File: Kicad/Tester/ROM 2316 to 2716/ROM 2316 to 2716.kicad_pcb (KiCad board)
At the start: 2 copper layers, 19.8 x 30.5 mm, 6 parts, among them IC1 74LVC1G04GV,125, J1 2316 Right, J2 2316 Left, J3 2716 Left, J4 2716 Right

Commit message: Renamed HCP65 Power to W65C816 Power.
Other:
- board text added: "2316 to 2716 ROM Adapter"
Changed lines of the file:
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@@
 			(outputformat 1)
 			(mirror no)
-			(drillshape 1)
+			(drillshape 0)
 			(scaleselection 1)
-			(outputdirectory "")
+			(outputdirectory "ROM 2316 to 2716/")
 		)
 	)
@@
 		(layer "Edge.Cuts")
 	)
+	(gr_text "2316 to 2716\nROM Adapter"
+		(at 90.043 73.279 90)
+		(layer "F.SilkS")
+		(effects
+			(font
+				(size 1 1)
+				(thickness 0.2)
+				(bold yes)
+			)
+		)
+	)
 	(segment
 		(start 90.17 84.328)
@@
 	)
 	(segment
-		(start 97.9243 63.5)
-		(end 98.552 63.5)
-		(width 0.35)
-		(layer "F.Cu")
-		(net 1)
-	)
-	(segment
-		(start 96.52 63.5)
-		(end 97.883 63.5)
-		(width 0.35)
-		(layer "F.Cu")
-		(net 1)
-	)
-	(segment
 		(start 95.504 69.85)
 		(end 97.282 69.85)
@@
 	)
 	(segment
+		(start 96.52 63.5)
+		(end 98.552 63.5)
+		(width 1.1)
+		(layer "F.Cu")
+		(net 1)
+	)
+	(segment
 		(start 90.17 83.643)
 		(end 91.009 82.804)
@@
 	)
 	(segment
-		(start 97.883 63.5)
-		(end 97.9243 63.5)
-		(width 0.35)
-		(layer "F.Cu")
-		(net 1)
-	)
-	(segment
 		(start 94.996 65.024)
 		(end 94.996 69.342)
@@
 		(start 83.312 91.44)
 		(end 81.28 91.44)
-		(width 0.35)
+		(width 1.1)
 		(layer "F.Cu")
 		(net 2)
@@
 		(start 98.552 68.58)
 		(end 96.52 68.58)
-		(width 0.2)
+		(width 1.1)
 		(layer "F.Cu")
 		(net 6)
@@
 		(start 83.312 78.74)
 		(end 81.28 78.74)
-		(width 0.2)
+		(width 1.1)
 		(layer "F.Cu")
 		(net 7)
@@
 		(start 83.312 68.58)
 		(end 81.28 68.58)
-		(width 0.2)
+		(width 1.1)
 		(layer "F.Cu")
 		(net 8)
@@
 		(start 83.312 73.66)
 		(end 81.28 73.66)
-		(width 0.2)
+		(width 1.1)
 		(layer "F.Cu")
 		(net 9)
@@
 		(start 83.312 71.12)
 		(end 81.28 71.12)
-		(width 0.2)
+		(width 1.1)
 		(layer "F.Cu")
 		(net 10)
@@
 		(start 81.28 83.82)
 		(end 83.312 83.82)
-		(width 0.2)
+		(width 1.1)
 		(layer "F.Cu")
 		(net 11)
@@
 		(start 96.52 73.66)
 		(end 98.552 73.66)
-		(width 0.2)
+		(width 1.1)
 		(layer "F.Cu")
 		(net 12)
@@
 		(start 96.520001 88.9)
 		(end 98.552001 88.9)
-		(width 0.2)
+		(width 1.1)
 		(layer "F.Cu")
 		(net 13)
@@
 		(start 96.52 91.44)
 		(end 98.552 91.44)
-		(width 0.2)
+		(width 1.1)
 		(layer "F.Cu")
 		(net 14)
@@
 		(start 83.312 76.2)
 		(end 81.28 76.2)
-		(width 0.2)
+		(width 1.1)
 		(layer "F.Cu")
 		(net 15)
@@
 		(start 81.28 63.5)
 		(end 83.312 63.5)
-		(width 0.2)
+		(width 1.1)
 		(layer "F.Cu")
 		(net 16)
@@
 		(start 83.312 86.36)
 		(end 81.28 86.36)
-		(width 0.2)
+		(width 1.1)
 		(layer "F.Cu")
 		(net 17)
@@
 		(start 98.552 83.82)
 		(end 96.52 83.82)
-		(width 0.2)
+		(width 1.1)
 		(layer "F.Cu")
 		(net 18)
@@
 		(start 96.520001 66.04)
 		(end 98.552001 66.04)
-		(width 0.2)
+		(width 1.1)
 		(layer "F.Cu")
 		(net 19)
@@
 		(start 98.552 76.199999)
 		(end 96.52 76.199999)
-		(width 0.2)
+		(width 1.1)
 		(layer "F.Cu")
 		(net 20)
@@
 		(start 81.28 81.28)
 		(end 83.312 81.28)
-		(width 0.2)
+		(width 1.1)
 		(layer "F.Cu")
 		(net 21)
@@
 		(start 83.312 88.9)
 		(end 81.28 88.9)
-		(width 0.2)
+		(width 1.1)
 		(layer "F.Cu")
 		(net 22)
@@
 		(start 98.552 81.28)
 		(end 96.52 81.28)
-		(width 0.2)
+		(width 1.1)
 		(layer "F.Cu")
 		(net 23)
@@
 		(start 98.552 86.36)
 		(end 96.52 86.36)
-		(width 0.2)
+		(width 1.1)
 		(layer "F.Cu")
 		(net 24)
@@
 		(start 81.28 66.04)
 		(end 83.312 66.04)
-		(width 0.2)
+		(width 1.1)
 		(layer "F.Cu")
 		(net 25)

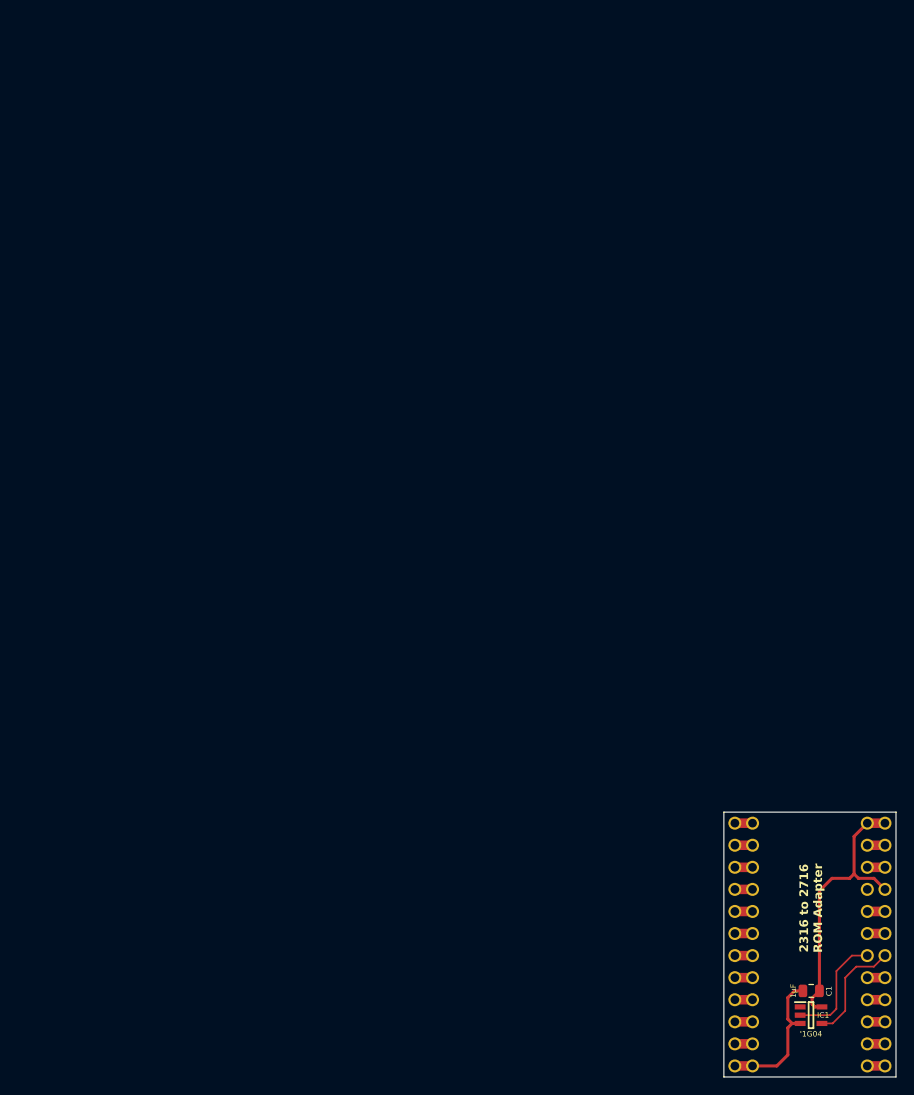
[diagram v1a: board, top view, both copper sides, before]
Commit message: Added RAM 48K Select.
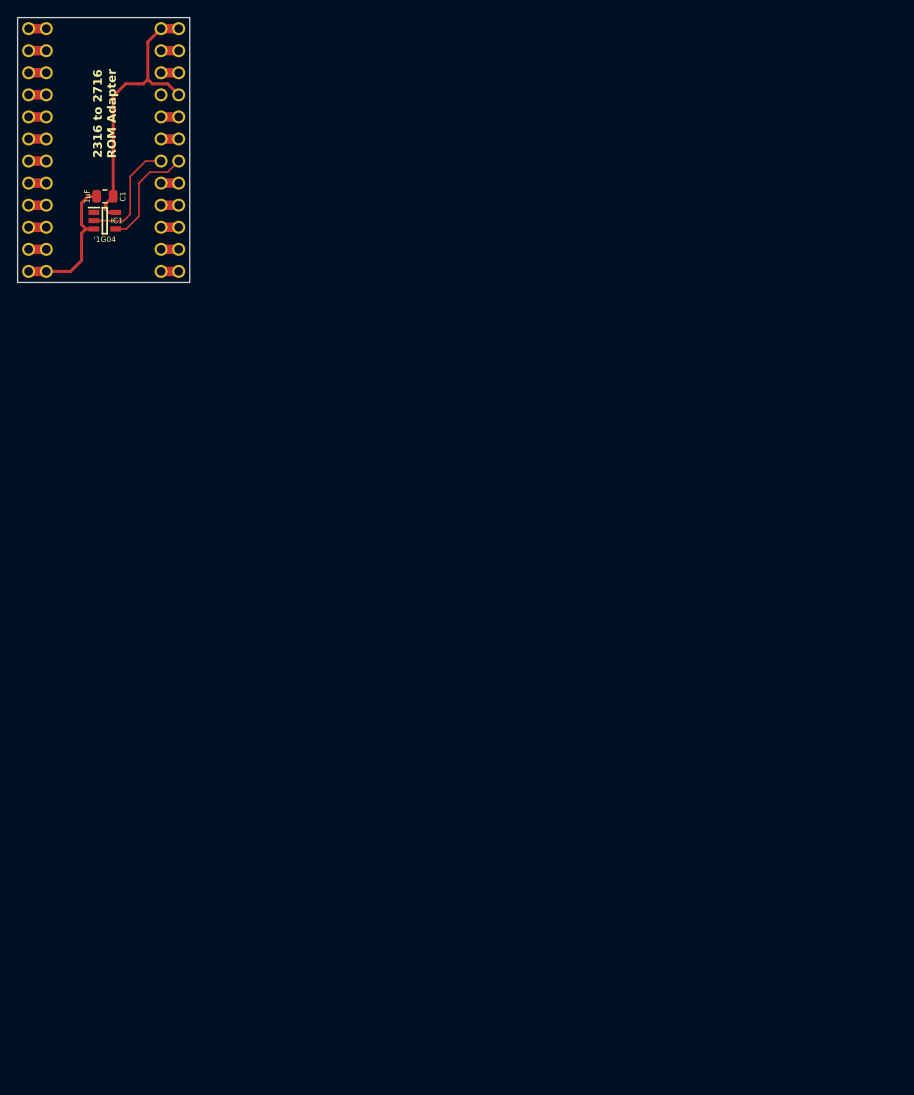
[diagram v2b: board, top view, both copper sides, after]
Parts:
- moved C1 122.3 mm to (8.76, -8.64)
- moved IC1 122.3 mm to (8.76, -5.84)
- moved J1 122.3 mm to (15.2, -27.9)
- moved J2 122.3 mm to (0.00, -27.9)
- moved J3 122.3 mm to (2.03, -27.9)
- moved J4 122.3 mm to (17.3, -27.9)

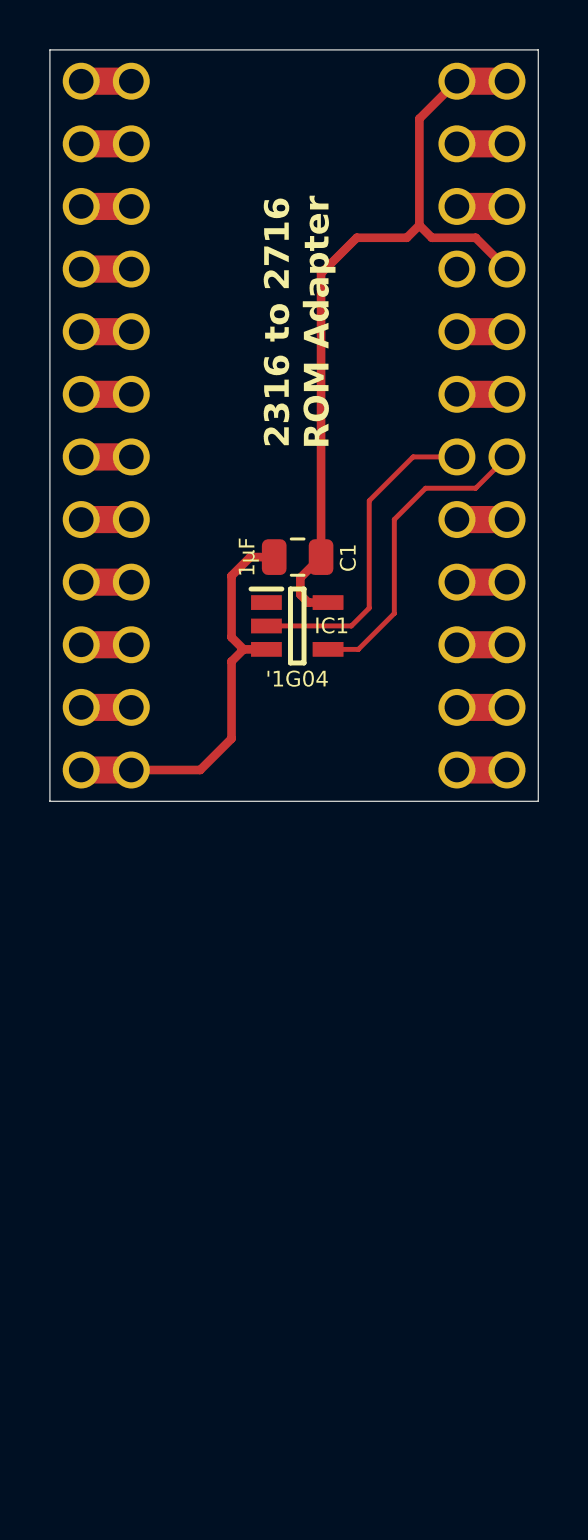
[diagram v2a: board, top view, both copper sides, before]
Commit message: Re-routed RAM 48K Select.
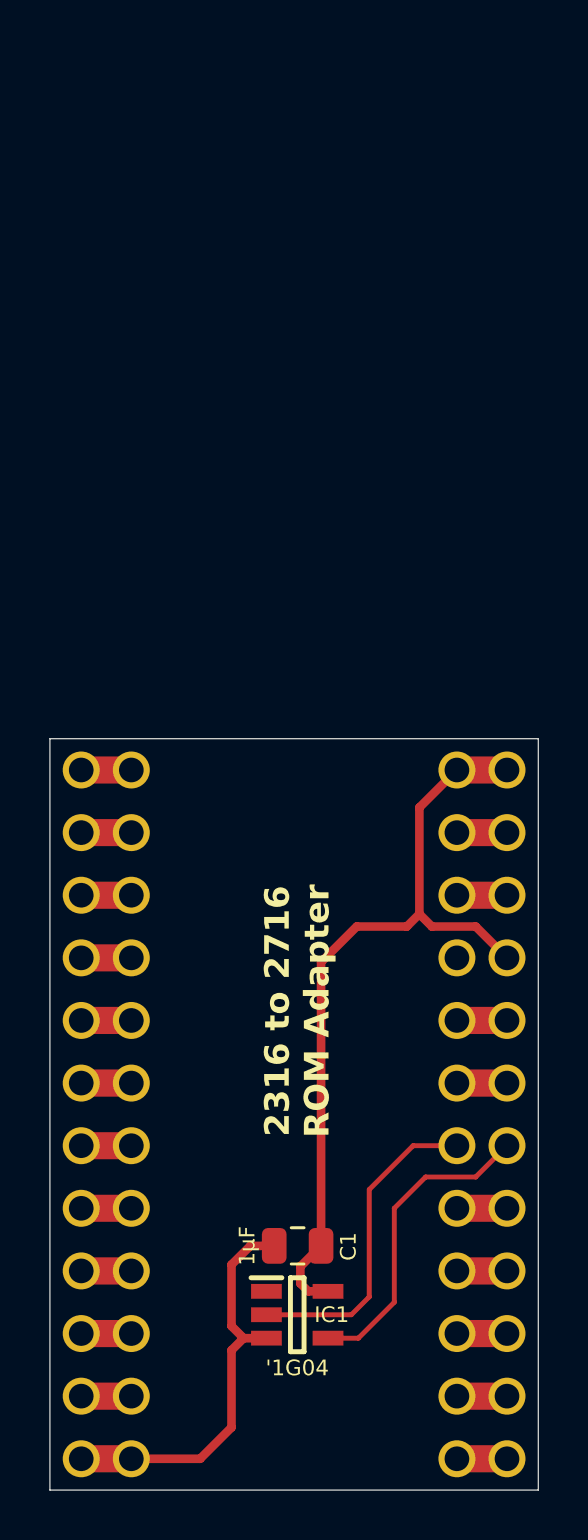
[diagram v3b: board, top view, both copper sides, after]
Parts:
- moved J1 27.9 mm to (15.2, 0.00)
- moved J2 27.9 mm to (0.00, 0.00)
- moved J3 27.9 mm to (2.03, 0.00)
- moved J4 27.9 mm to (17.3, 0.00)
- moved C1 27.9 mm to (8.76, 19.3)
- moved IC1 27.9 mm to (8.76, 22.1)
